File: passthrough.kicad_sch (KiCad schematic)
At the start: 14 parts, among them J10 MiniFit, J5 Pixhawk 1, J6 Pixhawk 2, U17 TLA2528

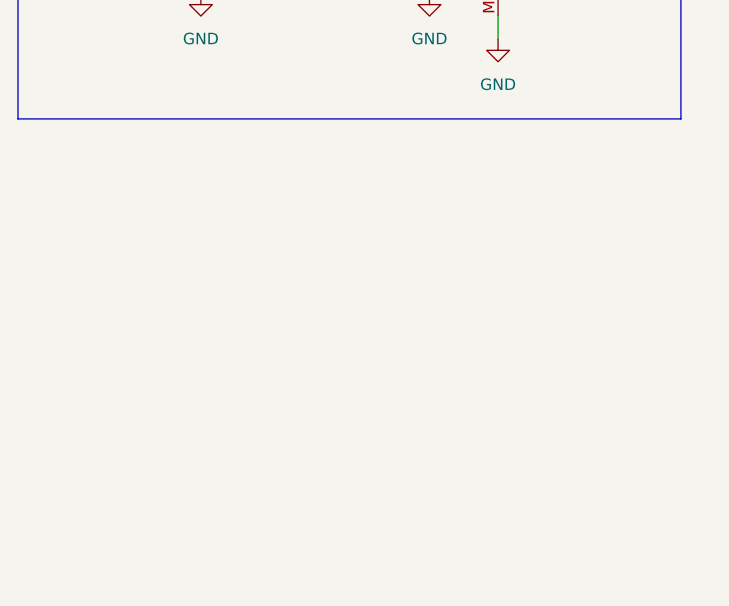
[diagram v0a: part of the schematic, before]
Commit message: fix capacitor sizes, clean up silkscreen, export
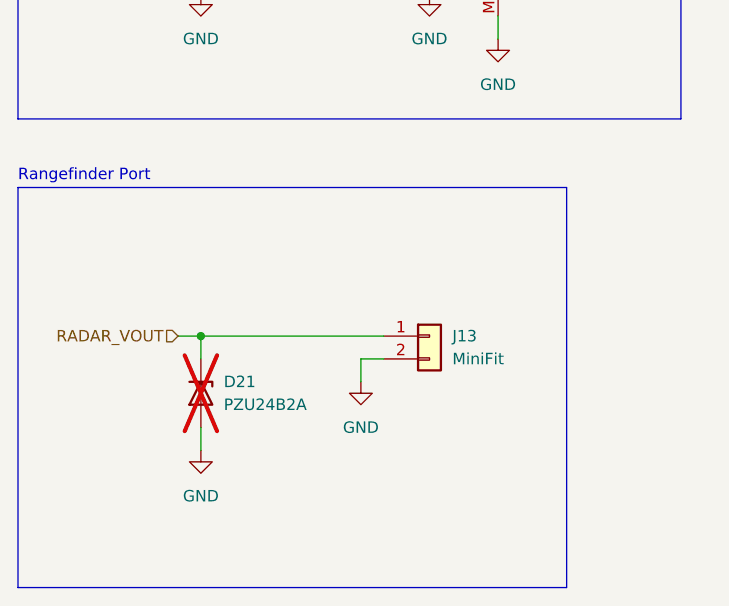
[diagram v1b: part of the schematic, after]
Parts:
- added D21: PZU24B2A, Diode_SMD:D_SOD-323F, symbol Device:D_Zener
- added J13: MiniFit, Connector_Molex:Molex_Mini-Fit_Jr_5569-02A2_2x01_P4.20mm_Horizontal, symbol Connector_Generic:Conn_01x02
- J10: footprint Connector_Molex:Molex_Mini-Fit_Jr_5569-04A1_2x02_P4.20mm_Horizontal -> Connector_Molex:Molex_Mini-Fit_Jr_5569-04A2_2x02_P4.20mm_Horizontal
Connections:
- net GND: now also D21.2 (A), J13.2 (Pin_2)
- new net RADAR_VOUT: D21.1 (K), J13.1 (Pin_1)
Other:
- note added: "Rangefinder Port"

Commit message: minor revisions
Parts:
- added R81: 220K 1%, Resistor_SMD:R_0603_1608Metric, symbol Device:R
- added R82: 1K, Resistor_SMD:R_0603_1608Metric, symbol Device:R
- added R83: 10K 1%, Resistor_SMD:R_0603_1608Metric, symbol Device:R
- added TP11: VBAT_SCALED, TestPoint:TestPoint_Pad_1.5x1.5mm, symbol Connector:TestPoint
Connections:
- net CM_VOUT: now also J10.3 (Pin_3), J10.4 (Pin_4); no longer J10.1 (Pin_1), J10.2 (Pin_2)
- net GND: now also J10.1 (Pin_1), J10.2 (Pin_2), J13.1 (Pin_1), R83.2; no longer J10.3 (Pin_3), J10.4 (Pin_4), J13.2 (Pin_2)
- net RADAR_VOUT: now also J13.2 (Pin_2); no longer J13.1 (Pin_1)
- net RESV2: now also R82.2, TP11.1
- new net: R81.2, R82.1, R83.1
- new net +BATT: R81.1
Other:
- note added: "Backup Voltage Sense"
